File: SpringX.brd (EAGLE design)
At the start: 21.3 x 15.2 mm, 9 parts, among them U1 MCP1703-5002E/CB, U2 MCP602ST

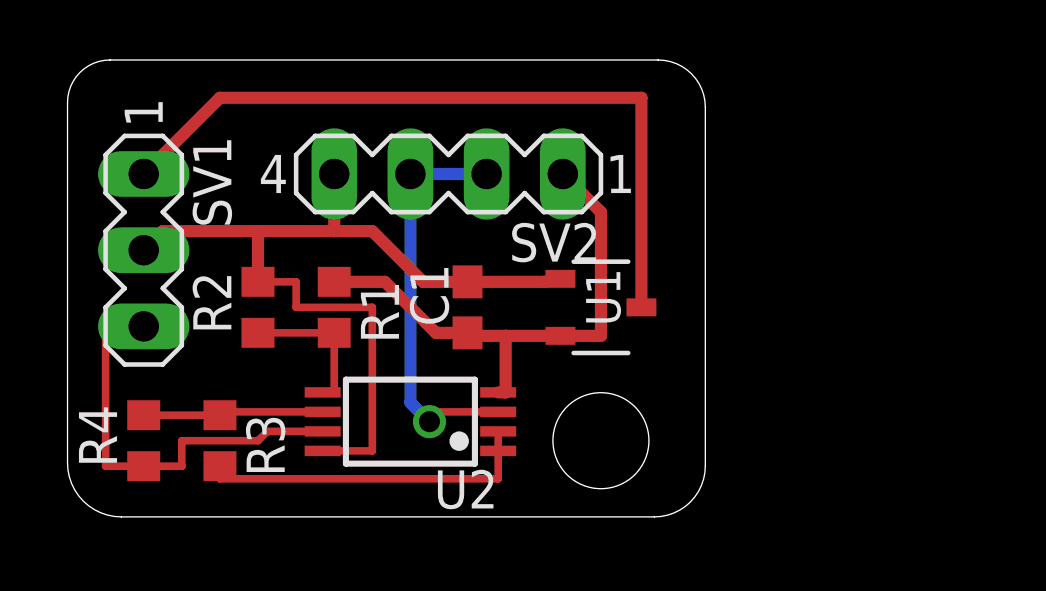
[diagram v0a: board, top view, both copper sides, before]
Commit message: Revised board layout to use solder pads for strain gauges and Molex PICO-SPOX connector for car interface.
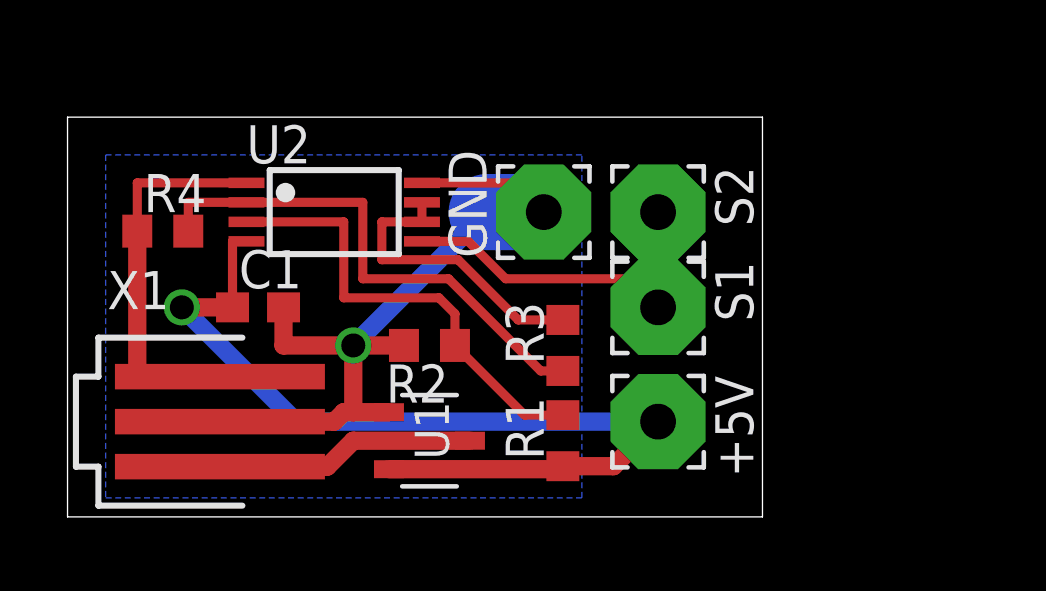
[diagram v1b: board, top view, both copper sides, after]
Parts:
- removed SV1: (no value), con-lstb:MA03-1
- removed SV2: (no value), con-lstb:MA04-1
- added +5V, GND, S1, S2: WIREPAD3,17/1,2, wirepad:3,17/1,2
- added X1: 87438-03, con-molex:87438-03
- C1: value (none) -> 1uF
- R1, R2, R3, R4: device resistor:R0603 -> rcl:R0603
- moved R3 11.9 mm to (16.5, 5.71), turned to 90 degrees
- moved R1 8.82 mm to (16.5, 2.54), turned to 90 degrees
- moved U2 7.43 mm to (8.89, 10.2), turned to 270 degrees
- moved U1 7.24 mm to (12.1, 2.54)
- moved R4 7.01 mm to (3.17, 9.53), turned to 0 degrees
- moved C1 6.99 mm to (6.35, 6.99), turned to 0 degrees
- moved R2 5.85 mm to (12.1, 5.71), turned to 180 degrees
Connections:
- net 5V: now also +5V.1; no longer SV2.1
- net GND: now also GND.1, X1.2; no longer SV1.2, SV2.4
- net N$1: now also X1.3; no longer SV1.1
- net N$2: now also U2.6, U2.7; no longer U2.1, U2.2
- net N$4: now also U2.2; no longer U2.6
- net OUT: now also U2.1, X1.1; no longer SV1.3, U2.7
- net STR: now also S1.1, S2.1, U2.5; no longer SV2.2, SV2.3, U2.3
- net VREF: now also U2.3; no longer U2.5
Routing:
- net N$1: track 24.6 -> 8.69 mm
- net 5V: track 17.8 -> 31.4 mm, vias 0 -> 1
- net N$4: track 6.01 -> 17.3 mm
- net VREF: track 4.91 -> 15.5 mm
- net GND: track 29.6 -> 26.1 mm, vias 0 -> 1
- net STR: track 13.5 -> 11.6 mm, vias 1 -> 0
- net OUT: track 14.1 -> 12.9 mm
- net N$2: track 11.3 -> 10.1 mm
- added copper zone on layer 16, net GND
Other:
- board size 21.3 x 15.2 mm -> 23.2 x 13.3 mm

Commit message: Re-arranged board layout to reduce width. This will allow the board to be passed through smaller holes in bodywork while permanently connected to the spring.
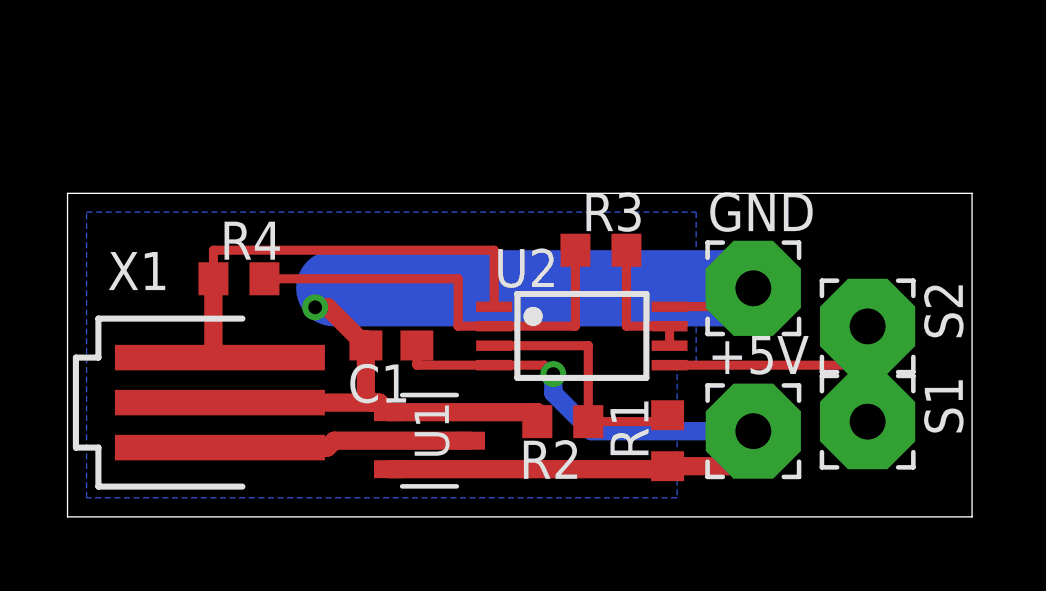
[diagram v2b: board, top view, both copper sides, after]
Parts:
- moved U2 9.23 mm to (17.1, 6.03)
- moved S1 7.96 mm to (26.7, 3.17)
- moved S2 7.96 mm to (26.7, 6.35)
- moved GND 7.43 mm to (22.9, 7.62), turned to 0 degrees
- moved R2 5.12 mm to (16.5, 3.17)
- moved C1 4.62 mm to (10.8, 5.71), turned to 180 degrees
- moved R1 3.49 mm to (20.0, 2.54)
- moved R3 3.42 mm to (17.8, 8.89), turned to 0 degrees
- moved +5V 3.19 mm to (22.9, 2.86), turned to 0 degrees
- moved R4 3.00 mm to (5.71, 7.94)
- moved X1 0.64 mm to (5.08, 3.81)
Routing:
- net GND: track 26.1 -> 33.4 mm
- net VREF: track 15.5 -> 8.53 mm
- net N$2: track 10.1 -> 4.62 mm
- net 5V: track 31.4 -> 26.0 mm
- net N$4: track 17.3 -> 14.5 mm
- net OUT: track 12.9 -> 15.0 mm
- net STR: track 11.6 -> 9.78 mm
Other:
- board size 23.2 x 13.3 mm -> 30.1 x 10.8 mm
